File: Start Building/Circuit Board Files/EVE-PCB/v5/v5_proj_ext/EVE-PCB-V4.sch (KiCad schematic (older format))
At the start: 8 parts, among them J1 Conn_02x09_Top_Bottom, J2 Conn_02x09_Top_Bottom, J3 Conn_02x09_Top_Bottom, J4 Conn_02x09_Top_Bottom, J6 Conn_02x18_Odd_Even, J7 Conn_02x22_Odd_Even

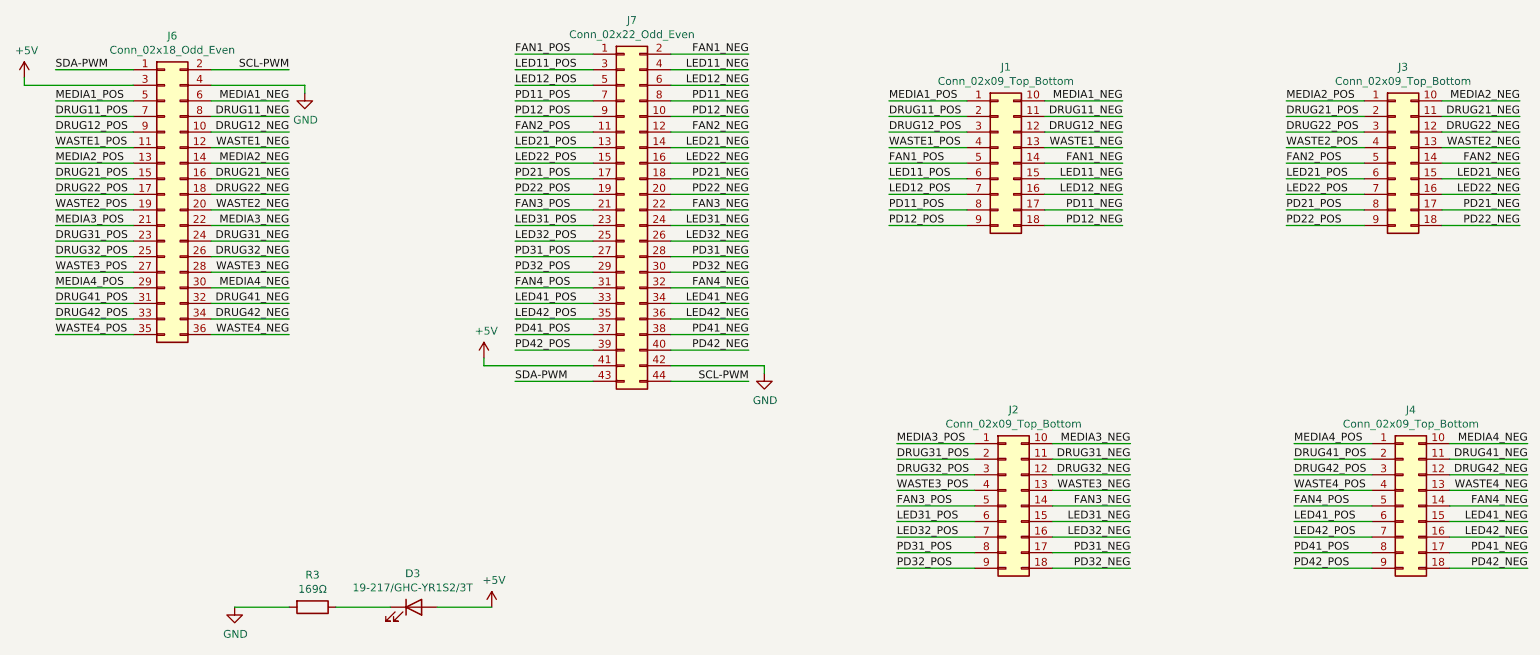
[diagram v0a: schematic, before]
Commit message: PCBv5 update some schematics
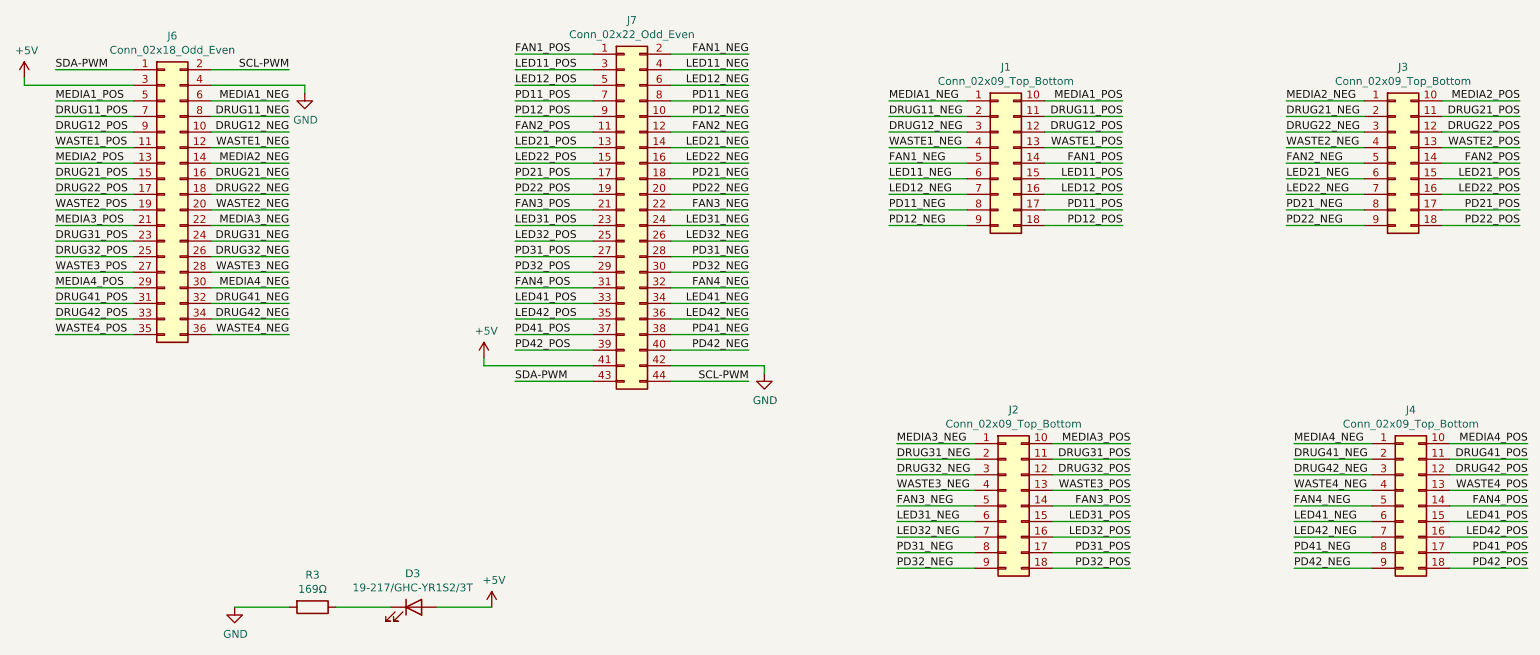
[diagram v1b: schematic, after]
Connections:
- net DRUG11_NEG: now also J1.2 (Pin_2); no longer J1.11 (Pin_11)
- net DRUG11_POS: now also J1.11 (Pin_11); no longer J1.2 (Pin_2)
- net DRUG12_NEG: now also J1.3 (Pin_3); no longer J1.12 (Pin_12)
- net DRUG12_POS: now also J1.12 (Pin_12); no longer J1.3 (Pin_3)
- net DRUG21_NEG: now also J3.2 (Pin_2); no longer J3.11 (Pin_11)
- net DRUG21_POS: now also J3.11 (Pin_11); no longer J3.2 (Pin_2)
- net DRUG22_NEG: now also J3.3 (Pin_3); no longer J3.12 (Pin_12)
- net DRUG22_POS: now also J3.12 (Pin_12); no longer J3.3 (Pin_3)
- net DRUG31_NEG: now also J2.2 (Pin_2); no longer J2.11 (Pin_11)
- net DRUG31_POS: now also J2.11 (Pin_11); no longer J2.2 (Pin_2)
- net DRUG32_NEG: now also J2.3 (Pin_3); no longer J2.12 (Pin_12)
- net DRUG32_POS: now also J2.12 (Pin_12); no longer J2.3 (Pin_3)
- net DRUG41_NEG: now also J4.2 (Pin_2); no longer J4.11 (Pin_11)
- net DRUG41_POS: now also J4.11 (Pin_11); no longer J4.2 (Pin_2)
- net DRUG42_NEG: now also J4.3 (Pin_3); no longer J4.12 (Pin_12)
- net DRUG42_POS: now also J4.12 (Pin_12); no longer J4.3 (Pin_3)
- net FAN1_NEG: now also J1.5 (Pin_5); no longer J1.14 (Pin_14)
- net FAN1_POS: now also J1.14 (Pin_14); no longer J1.5 (Pin_5)
- net FAN2_NEG: now also J3.5 (Pin_5); no longer J3.14 (Pin_14)
- net FAN2_POS: now also J3.14 (Pin_14); no longer J3.5 (Pin_5)
- net FAN3_NEG: now also J2.5 (Pin_5); no longer J2.14 (Pin_14)
- net FAN3_POS: now also J2.14 (Pin_14); no longer J2.5 (Pin_5)
- net FAN4_NEG: now also J4.5 (Pin_5); no longer J4.14 (Pin_14)
- net FAN4_POS: now also J4.14 (Pin_14); no longer J4.5 (Pin_5)
- net LED11_NEG: now also J1.6 (Pin_6); no longer J1.15 (Pin_15)
- net LED11_POS: now also J1.15 (Pin_15); no longer J1.6 (Pin_6)
- net LED12_NEG: now also J1.7 (Pin_7); no longer J1.16 (Pin_16)
- net LED12_POS: now also J1.16 (Pin_16); no longer J1.7 (Pin_7)
- net LED21_NEG: now also J3.6 (Pin_6); no longer J3.15 (Pin_15)
- net LED21_POS: now also J3.15 (Pin_15); no longer J3.6 (Pin_6)
- net LED22_NEG: now also J3.7 (Pin_7); no longer J3.16 (Pin_16)
- net LED22_POS: now also J3.16 (Pin_16); no longer J3.7 (Pin_7)
- net LED31_NEG: now also J2.6 (Pin_6); no longer J2.15 (Pin_15)
- net LED31_POS: now also J2.15 (Pin_15); no longer J2.6 (Pin_6)
- net LED32_NEG: now also J2.7 (Pin_7); no longer J2.16 (Pin_16)
- net LED32_POS: now also J2.16 (Pin_16); no longer J2.7 (Pin_7)
- net LED41_NEG: now also J4.6 (Pin_6); no longer J4.15 (Pin_15)
- net LED41_POS: now also J4.15 (Pin_15); no longer J4.6 (Pin_6)
- net LED42_NEG: now also J4.7 (Pin_7); no longer J4.16 (Pin_16)
- net LED42_POS: now also J4.16 (Pin_16); no longer J4.7 (Pin_7)
- net MEDIA1_NEG: now also J1.1 (Pin_1); no longer J1.10 (Pin_10)
- net MEDIA1_POS: now also J1.10 (Pin_10); no longer J1.1 (Pin_1)
- net MEDIA2_NEG: now also J3.1 (Pin_1); no longer J3.10 (Pin_10)
- net MEDIA2_POS: now also J3.10 (Pin_10); no longer J3.1 (Pin_1)
- net MEDIA3_NEG: now also J2.1 (Pin_1); no longer J2.10 (Pin_10)
- net MEDIA3_POS: now also J2.10 (Pin_10); no longer J2.1 (Pin_1)
- net MEDIA4_NEG: now also J4.1 (Pin_1); no longer J4.10 (Pin_10)
- net MEDIA4_POS: now also J4.10 (Pin_10); no longer J4.1 (Pin_1)
- net PD11_NEG: now also J1.8 (Pin_8); no longer J1.17 (Pin_17)
- net PD11_POS: now also J1.17 (Pin_17); no longer J1.8 (Pin_8)
- net PD12_NEG: now also J1.9 (Pin_9); no longer J1.18 (Pin_18)
- net PD12_POS: now also J1.18 (Pin_18); no longer J1.9 (Pin_9)
- net PD21_NEG: now also J3.8 (Pin_8); no longer J3.17 (Pin_17)
- net PD21_POS: now also J3.17 (Pin_17); no longer J3.8 (Pin_8)
- net PD22_NEG: now also J3.9 (Pin_9); no longer J3.18 (Pin_18)
- net PD22_POS: now also J3.18 (Pin_18); no longer J3.9 (Pin_9)
- net PD31_NEG: now also J2.8 (Pin_8); no longer J2.17 (Pin_17)
- net PD31_POS: now also J2.17 (Pin_17); no longer J2.8 (Pin_8)
- net PD32_NEG: now also J2.9 (Pin_9); no longer J2.18 (Pin_18)
- net PD32_POS: now also J2.18 (Pin_18); no longer J2.9 (Pin_9)
- net PD41_NEG: now also J4.8 (Pin_8); no longer J4.17 (Pin_17)
- net PD41_POS: now also J4.17 (Pin_17); no longer J4.8 (Pin_8)
- net PD42_NEG: now also J4.9 (Pin_9); no longer J4.18 (Pin_18)
- net PD42_POS: now also J4.18 (Pin_18); no longer J4.9 (Pin_9)
- net WASTE1_NEG: now also J1.4 (Pin_4); no longer J1.13 (Pin_13)
- net WASTE1_POS: now also J1.13 (Pin_13); no longer J1.4 (Pin_4)
- net WASTE2_NEG: now also J3.4 (Pin_4); no longer J3.13 (Pin_13)
- net WASTE2_POS: now also J3.13 (Pin_13); no longer J3.4 (Pin_4)
- net WASTE3_NEG: now also J2.4 (Pin_4); no longer J2.13 (Pin_13)
- net WASTE3_POS: now also J2.13 (Pin_13); no longer J2.4 (Pin_4)
- net WASTE4_NEG: now also J4.4 (Pin_4); no longer J4.13 (Pin_13)
- net WASTE4_POS: now also J4.13 (Pin_13); no longer J4.4 (Pin_4)
